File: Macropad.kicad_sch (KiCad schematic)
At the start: 1 part, among them U1 ESP8266EX

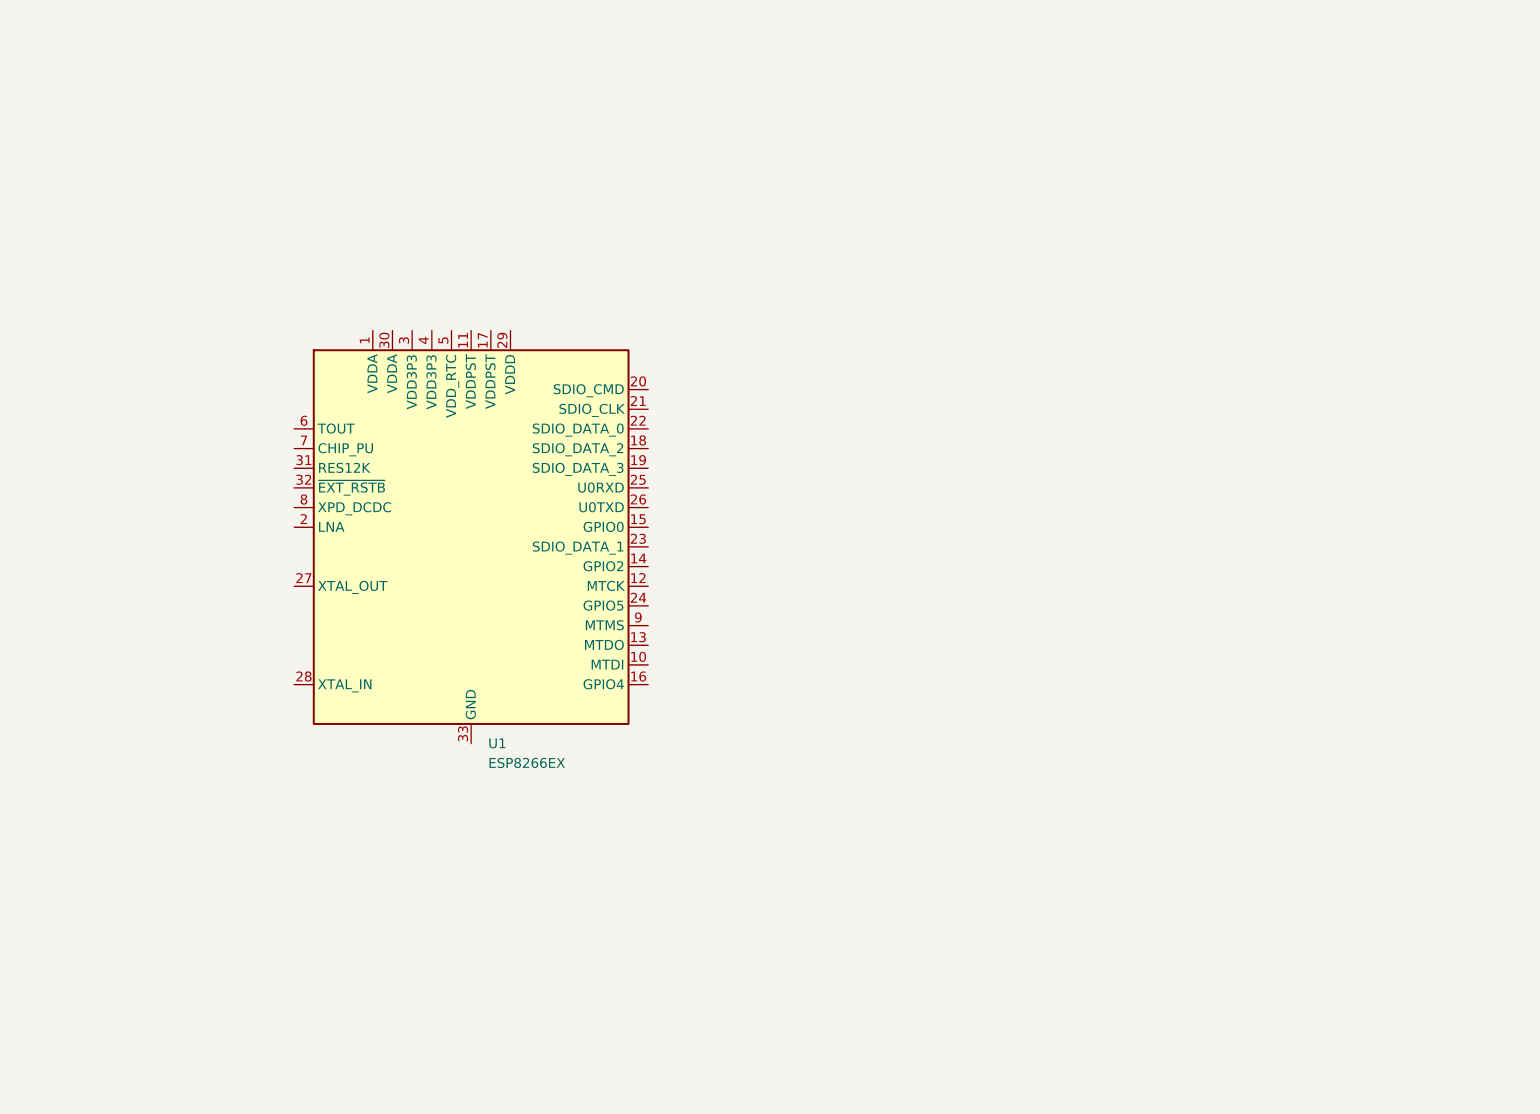
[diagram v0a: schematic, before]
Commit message: Schematic capture
Schematic for the 3x3 macropad has been finished (did not add the rows and columns to the MCU).
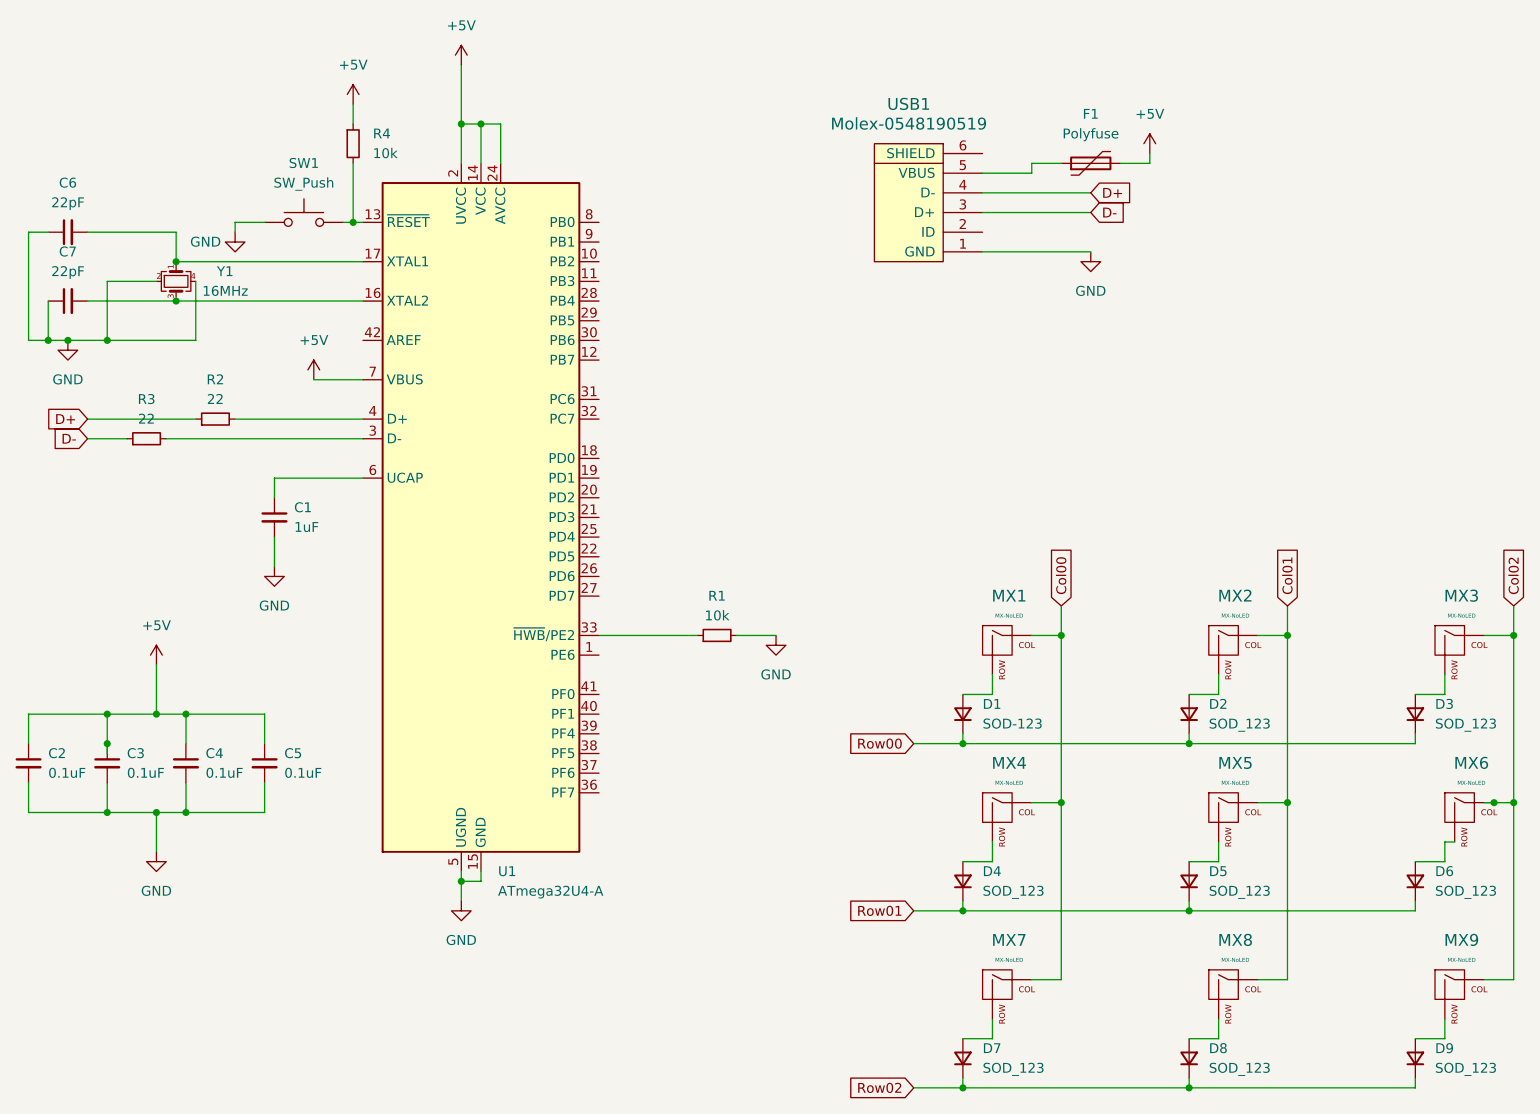
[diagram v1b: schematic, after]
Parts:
- removed U1: ESP8266EX, Package_DFN_QFN:QFN-32-1EP_5x5mm_P0.5mm_EP3.45x3.45mm, symbol MCU_Espressif:ESP8266EX
- added C1: 1uF, Capacitor_SMD:C_0805_2012Metric, symbol Device:C_Small
- added C2, C3, C4, C5: 0.1uF, Capacitor_SMD:C_0805_2012Metric, symbol Device:C_Small
- added C6, C7: 22pF, Capacitor_SMD:C_0805_2012Metric, symbol Device:C_Small
- added D1: SOD-123, Diode_SMD:D_SOD-123, symbol Device:D_Small
- added D2, D3, D4, D5, D6, D7, D8, D9: SOD_123, Diode_SMD:D_SOD-123, symbol Device:D_Small
- added F1: Polyfuse, Fuse:Fuse_1206_3216Metric, symbol Device:Polyfuse
- added MX1, MX2, MX3, MX4, MX5, MX6, MX7, MX8, MX9: MX-NoLED, MX_Alps_Hybrid:MX-1U-NoLED, symbol MX_Alps_Hybrid:MX-NoLED
- added R1, R4: 10k, Resistor_SMD:R_0805_2012Metric, symbol Device:R_Small
- added R2, R3: 22, Resistor_SMD:R_0805_2012Metric, symbol Device:R_Small
- added SW1: SW_Push, random-keyboard-parts:SKQG-1155865, symbol Switch:SW_Push
- added U1: ATmega32U4-A, Package_QFP:TQFP-44_10x10mm_P0.8mm, symbol MCU_Microchip_ATmega:ATmega32U4-A
- added USB1: Molex-0548190519, random-keyboard-parts:Molex-0548190589, symbol random-keyboard-parts:Molex-0548190519
- added Y1: 16MHz, Crystal:Crystal_SMD_3225-4Pin_3.2x2.5mm, symbol Device:Crystal_GND24_Small
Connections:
- new net: D1.2 (A), MX1.2 (ROW)
- new net: R4.2, SW1.2, U1.13 (~{RESET})
- new net: C7.2, U1.16 (XTAL2), Y1.3
- new net: C6.2, U1.17 (XTAL1), Y1.1
- new net: R3.2, U1.3 (D-)
- new net: R1.1, U1.33 (~{HWB}/PE2)
- new net: R2.2, U1.4 (D+)
- new net: C1.1, U1.6 (UCAP)
- new net: D6.2 (A), MX6.2 (ROW)
- new net: D5.2 (A), MX5.2 (ROW)
- new net: D2.2 (A), MX2.2 (ROW)
- new net: D9.2 (A), MX9.2 (ROW)
- new net: D4.2 (A), MX4.2 (ROW)
- new net: D3.2 (A), MX3.2 (ROW)
- new net: F1.1, USB1.5 (VBUS)
- new net: D8.2 (A), MX8.2 (ROW)
- new net: D7.2 (A), MX7.2 (ROW)
- new net +5V: C2.1, C3.1, C4.1, C5.1, F1.2, R4.1, U1.14 (VCC), U1.2 (UVCC), U1.24 (AVCC), U1.34 (VCC), U1.44 (AVCC), U1.7 (VBUS)
- new net Col00: MX1.1 (COL), MX4.1 (COL), MX7.1 (COL)
- new net Col01: MX2.1 (COL), MX5.1 (COL), MX8.1 (COL)
- new net Col02: MX3.1 (COL), MX6.1 (COL), MX9.1 (COL)
- new net D+: R2.1, USB1.4 (D-)
- new net D-: R3.1, USB1.3 (D+)
- new net GND: C1.2, C2.2, C3.2, C4.2, C5.2, C6.1, C7.1, R1.2, SW1.1, U1.15 (GND), U1.23 (GND), U1.35 (GND), U1.43 (GND), U1.5 (UGND), USB1.1 (GND), Y1.2, Y1.4
- new net Row00: D1.1 (K), D2.1 (K), D3.1 (K)
- new net Row01: D4.1 (K), D5.1 (K), D6.1 (K)
- new net Row02: D7.1 (K), D8.1 (K), D9.1 (K)

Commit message: routing of the components
pcb layout done
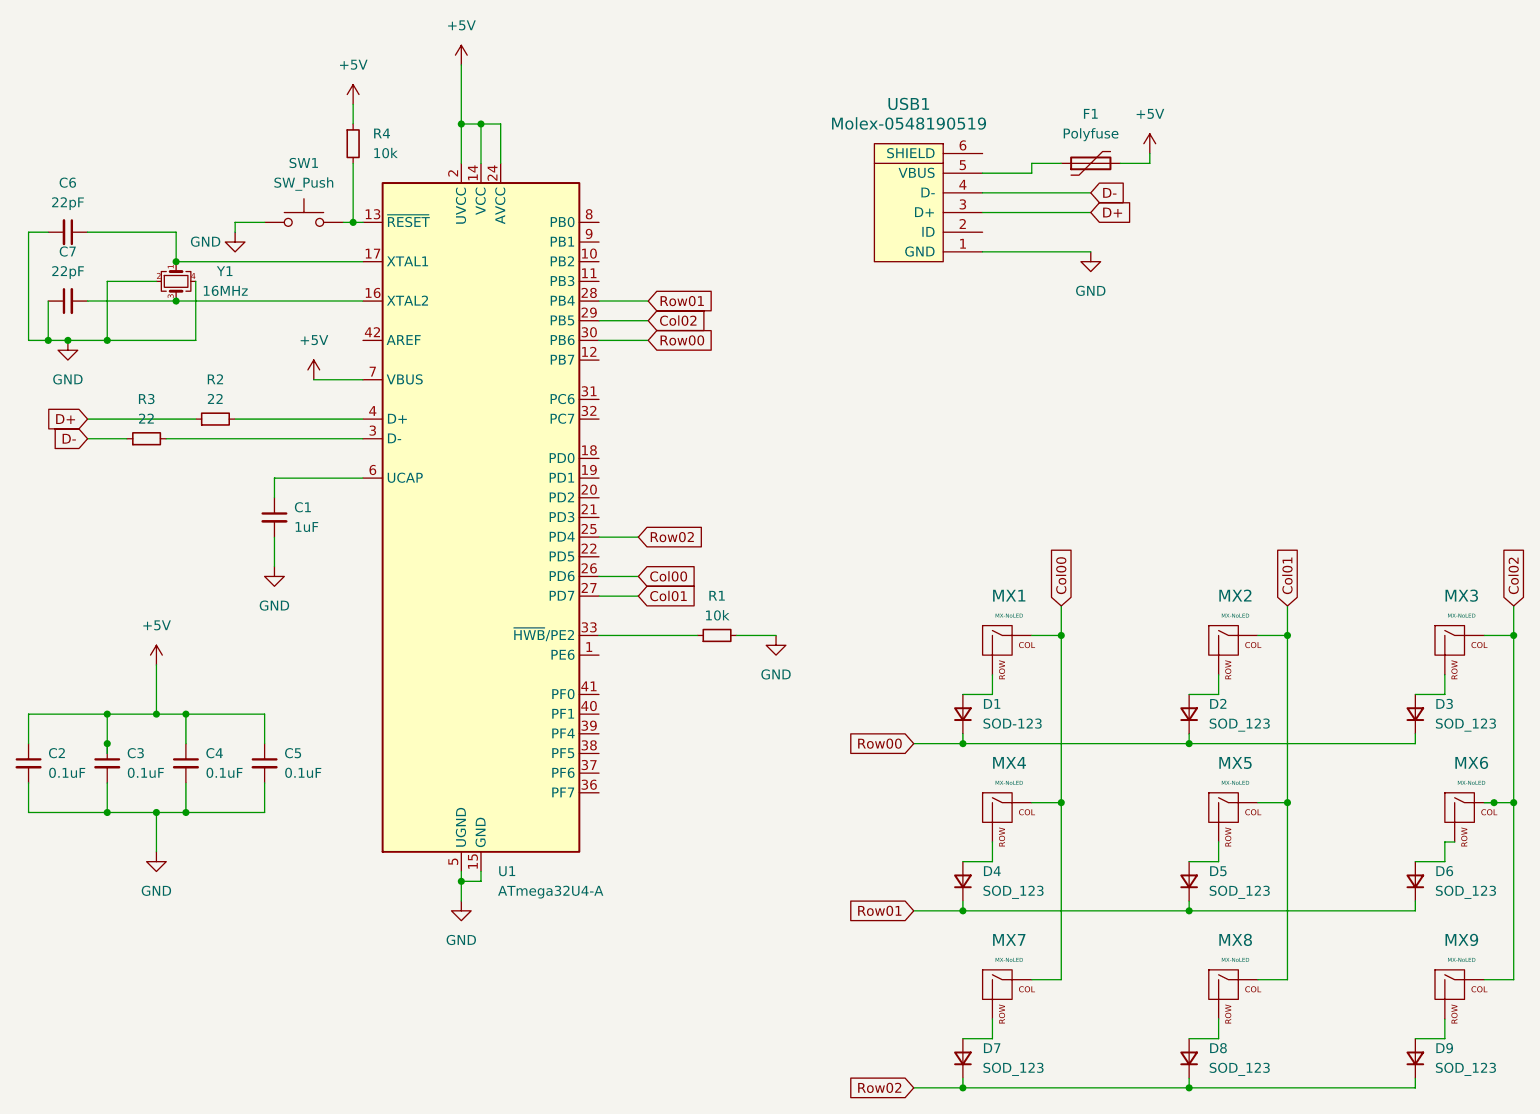
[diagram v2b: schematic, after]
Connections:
- net Col00: now also U1.26 (PD6)
- net Col01: now also U1.27 (PD7)
- net Col02: now also U1.29 (PB5)
- net D+: now also USB1.3 (D+); no longer USB1.4 (D-)
- net D-: now also USB1.4 (D-); no longer USB1.3 (D+)
- net GND: now also C6.2; no longer C6.1
- net Row00: now also U1.30 (PB6)
- net Row01: now also U1.28 (PB4)
- net Row02: now also U1.25 (PD4)
- net at U1.17 (XTAL1), Y1.1: now also C6.1; no longer C6.2
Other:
- moved on the sheet: C6
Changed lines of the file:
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@@
+    (stroke (width 0) (type default))
+  )
+  (wire (pts (xy 154.94 91.44) (xy 160.02 91.44))
     (stroke (width 0) (type default))
   )
@@
     (stroke (width 0) (type default))
   )
+  (wire (pts (xy 154.94 60.96) (xy 161.29 60.96))
+    (stroke (width 0) (type default))
+  )
   (wire (pts (xy 243.84 120.65) (xy 243.84 143.51))
     (stroke (width 0) (type default))
@@
     (stroke (width 0) (type default))
   )
+  (wire (pts (xy 154.94 86.36) (xy 160.02 86.36))
+    (stroke (width 0) (type default))
+  )
   (wire (pts (xy 273.05 99.06) (xy 273.05 120.65))
     (stroke (width 0) (type default))
@@
     (stroke (width 0) (type default))
   )
+  (wire (pts (xy 154.94 58.42) (xy 161.29 58.42))
+    (stroke (width 0) (type default))
+  )
   (wire (pts (xy 137.16 25.4) (xy 137.16 33.02))
     (stroke (width 0) (type default))
@@
     (stroke (width 0) (type default))
   )
+  (wire (pts (xy 154.94 55.88) (xy 161.29 55.88))
+    (stroke (width 0) (type default))
+  )
   (wire (pts (xy 264.16 128.27) (xy 260.35 128.27))
     (stroke (width 0) (type default))
@@
     (stroke (width 0) (type default))
   )
+  (wire (pts (xy 154.94 93.98) (xy 160.02 93.98))
+    (stroke (width 0) (type default))
+  )
   (wire (pts (xy 201.93 134.62) (xy 231.14 134.62))
     (stroke (width 0) (type default))
@@
   (wire (pts (xy 260.35 157.48) (xy 260.35 156.21))
     (stroke (width 0) (type default))
+  )
+  (global_label "Col00" (shape input) (at 160.02 91.44 0) (fields_autoplaced)
+    (effects (font (size 1.27 1.27)) (justify left))
+    (property "Intersheetrefs" "${INTERSHEET_REFS}" (at 168.5084 91.44 0)
+      (effects (font (size 1.27 1.27)) (justify left) hide)
+    )
+  )
+  (global_label "Row01" (shape input) (at 161.29 55.88 0) (fields_autoplaced)
+    (effects (font (size 1.27 1.27)) (justify left))
+    (property "Intersheetrefs" "${INTERSHEET_REFS}" (at 170.4437 55.88 0)
+      (effects (font (size 1.27 1.27)) (justify left) hide)
+    )
   )
   (global_label "Row01" (shape input) (at 195.58 134.62 180) (fields_autoplaced)
@@
     )
   )
+  (global_label "Row00" (shape input) (at 161.29 60.96 0) (fields_autoplaced)
+    (effects (font (size 1.27 1.27)) (justify left))
+    (property "Intersheetrefs" "${INTERSHEET_REFS}" (at 170.4437 60.96 0)
+      (effects (font (size 1.27 1.27)) (justify left) hide)
+    )
+  )
   (global_label "D+" (shape input) (at 88.9 71.12 180) (fields_autoplaced)
     (effects (font (size 1.27 1.27)) (justify right))
@@
     )
   )
-  (global_label "D-" (shape input) (at 218.44 44.45 0) (fields_autoplaced)
-    (effects (font (size 1.27 1.27)) (justify left))
-    (property "Intersheetrefs" "${INTERSHEET_REFS}" (at 224.2676 44.45 0)
-      (effects (font (size 1.27 1.27)) (justify left) hide)
-    )
-  )
   (global_label "D-" (shape input) (at 88.9 73.66 180) (fields_autoplaced)
     (effects (font (size 1.27 1.27)) (justify right))
@@
     )
   )
+  (global_label "D-" (shape input) (at 218.44 41.91 0) (fields_autoplaced)
+    (effects (font (size 1.27 1.27)) (justify left))
+    (property "Intersheetrefs" "${INTERSHEET_REFS}" (at 224.2676 41.91 0)
+      (effects (font (size 1.27 1.27)) (justify left) hide)
+    )
+  )
   (global_label "Col02" (shape input) (at 273.05 95.25 90) (fields_autoplaced)
     (effects (font (size 1.27 1.27)) (justify left))
@@
     )
   )
-  (global_label "D+" (shape input) (at 218.44 41.91 0) (fields_autoplaced)
+  (global_label "Col01" (shape input) (at 160.02 93.98 0) (fields_autoplaced)
     (effects (font (size 1.27 1.27)) (justify left))
-    (property "Intersheetrefs" "${INTERSHEET_REFS}" (at 224.2676 41.91 0)
+    (property "Intersheetrefs" "${INTERSHEET_REFS}" (at 168.5084 93.98 0)
+      (effects (font (size 1.27 1.27)) (justify left) hide)
+    )
+  )
+  (global_label "D+" (shape input) (at 218.44 44.45 0) (fields_autoplaced)
+    (effects (font (size 1.27 1.27)) (justify left))
+    (property "Intersheetrefs" "${INTERSHEET_REFS}" (at 224.2676 44.45 0)
+      (effects (font (size 1.27 1.27)) (justify left) hide)
+    )
+  )
+  (global_label "Col02" (shape input) (at 161.29 58.42 0) (fields_autoplaced)
+    (effects (font (size 1.27 1.27)) (justify left))
+    (property "Intersheetrefs" "${INTERSHEET_REFS}" (at 169.7784 58.42 0)
+      (effects (font (size 1.27 1.27)) (justify left) hide)
+    )
+  )
+  (global_label "Row02" (shape input) (at 160.02 86.36 0) (fields_autoplaced)
+    (effects (font (size 1.27 1.27)) (justify left))
+    (property "Intersheetrefs" "${INTERSHEET_REFS}" (at 169.1737 86.36 0)
       (effects (font (size 1.27 1.27)) (justify left) hide)
     )
@@
     )
   )
-  (symbol (lib_id "Device:C_Small") (at 86.36 46.99 90) (unit 1)
-    (in_bom yes) (on_board yes) (dnp no) (fields_autoplaced)
-    (property "Reference" "C6" (at 86.3663 40.64 90)
-      (effects (font (size 1.27 1.27)))
-    )
-    (property "Value" "22pF" (at 86.3663 43.18 90)
-      (effects (font (size 1.27 1.27)))
-    )
+  (symbol (lib_id "Device:C_Small") (at 86.36 46.99 270) (mirror x) (unit 1)
+    (in_bom yes) (on_board yes) (dnp no)
+    (property "Reference" "C6" (at 86.3537 40.64 90)
+      (effects (font (size 1.27 1.27)))
+    )
+    (property "Value" "22pF" (at 86.3537 43.18 90)
+      (effects (font (size 1.27 1.27)))
+    )
